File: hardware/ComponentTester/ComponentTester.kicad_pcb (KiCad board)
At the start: 2 copper layers, 51 x 90.6 mm, 18 parts, among them J1 Conn_01x06_Socket, J2 AVR-ISP-6, J3 Conn_02x07_Counter_Clockwise, J4 GameBoy_GamePak_DMG-09, SW1 SW_Push, U1 ATmega328P-A, X1 16MHz

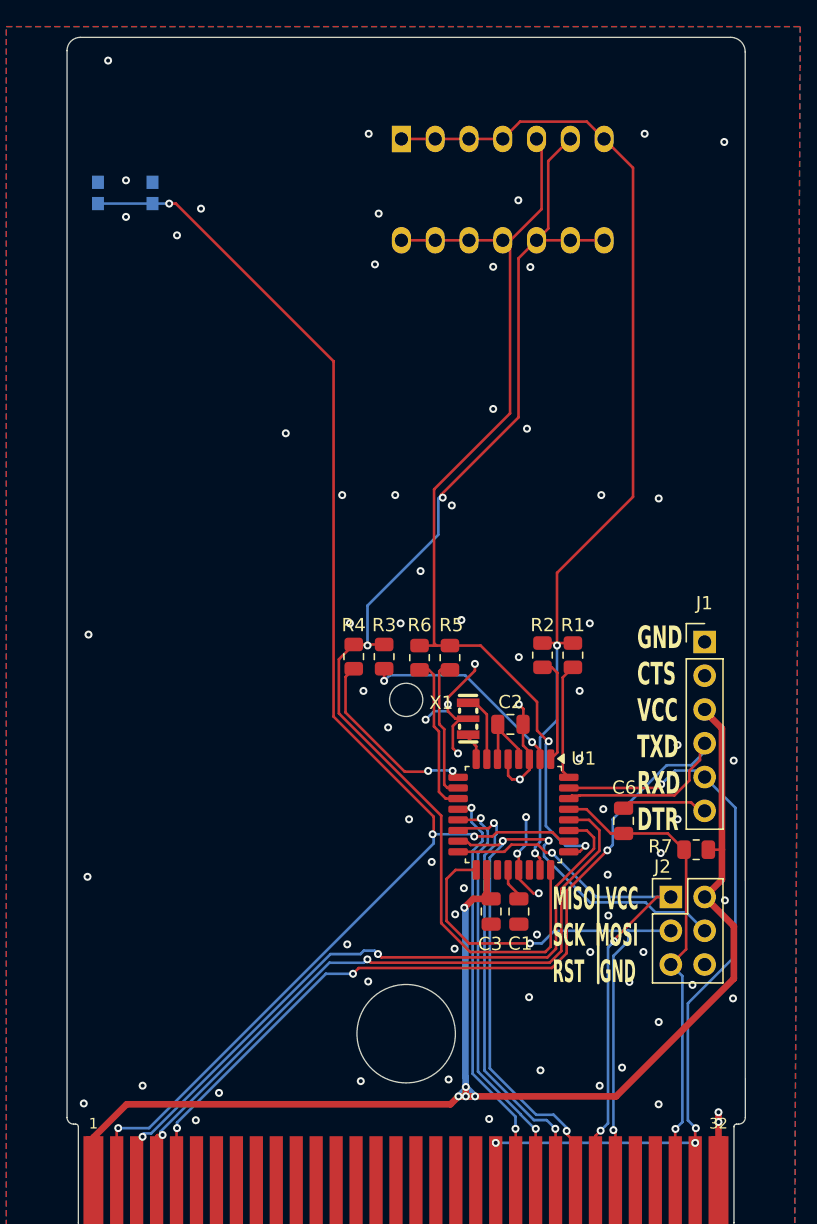
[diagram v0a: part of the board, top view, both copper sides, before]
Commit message: use ADC6 + ADC7
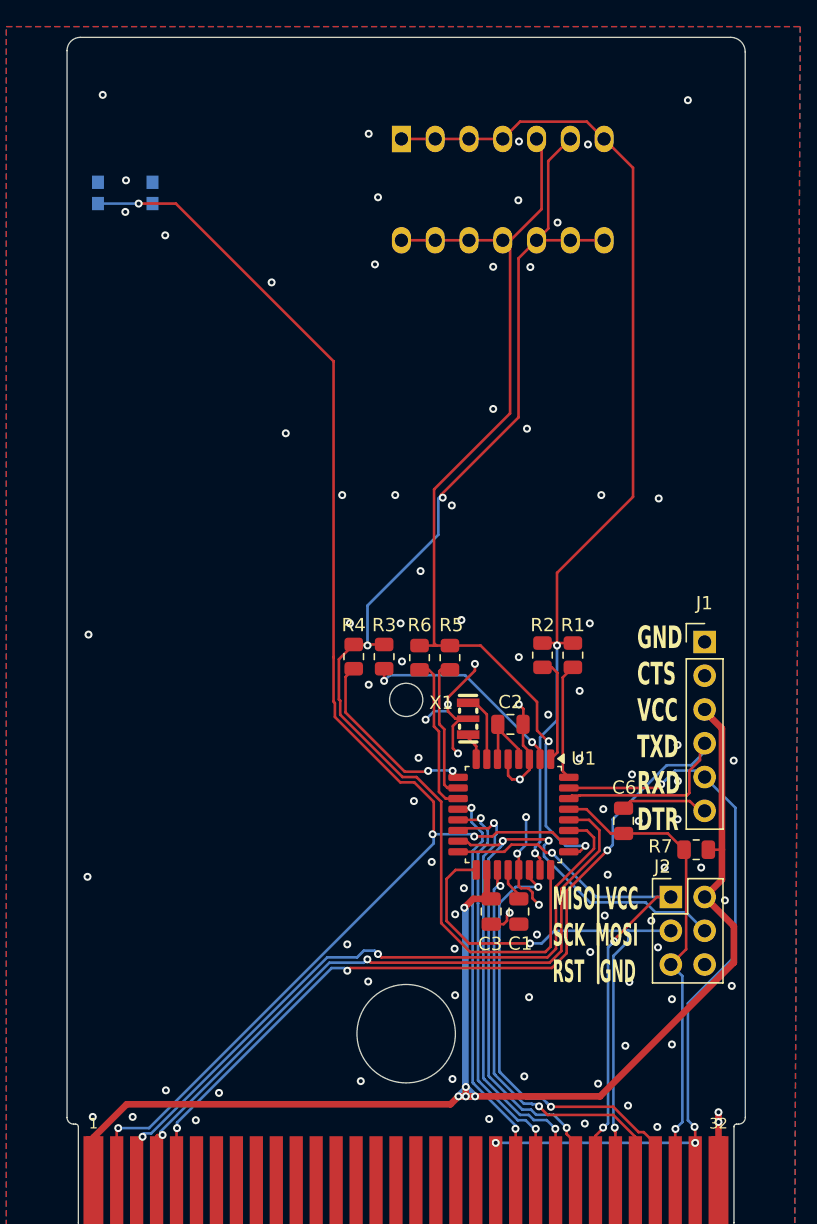
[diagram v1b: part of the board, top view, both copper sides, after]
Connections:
- U1 pad 19: unconnected-(U1-ADC6-Pad19) -> /CARD_D6
- U1 pad 22: unconnected-(U1-ADC7-Pad22) -> /CARD_D7
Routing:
- net /CARD_D7: track 0.00 -> 31.6 mm, vias 0 -> 2
- net /CARD_D6: track 0.00 -> 28.9 mm, vias 0 -> 2
- net GND: track 29.8 -> 32.7 mm, vias 78 -> 92
- net /CARD_~{CS}: track 69.9 -> 70.6 mm
- net /CARD_CLK: track 106.5 -> 107.1 mm
- net /2: track 91.8 -> 92.4 mm
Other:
- board text added: "Flash and program: https://electronoobs.com/eng_arduino_tut33.php https://wolles-elektronikkiste.de/atmega328p-standalone-betreiben"
- board text removed: "Flash and progran: https://electronoobs.com/eng_arduino_tut33.php"

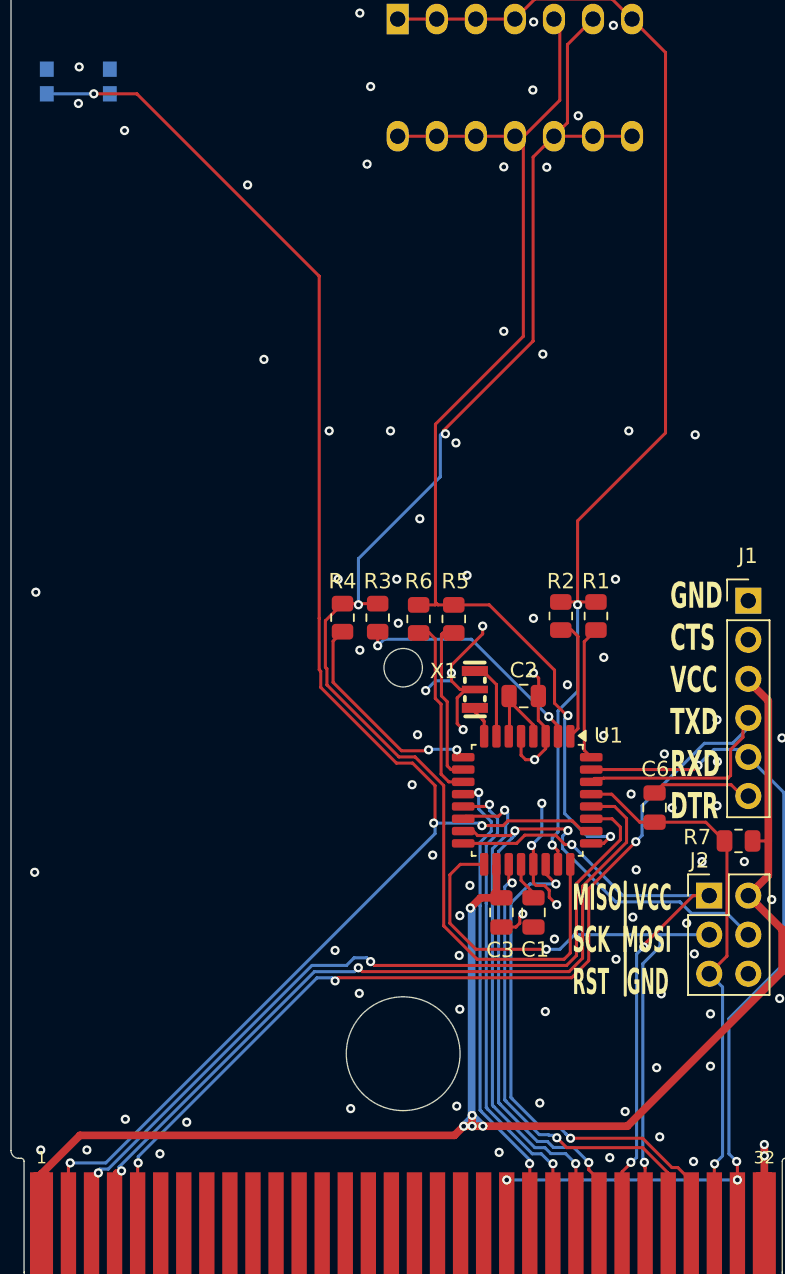
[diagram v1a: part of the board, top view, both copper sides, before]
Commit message: remove ext. crystal
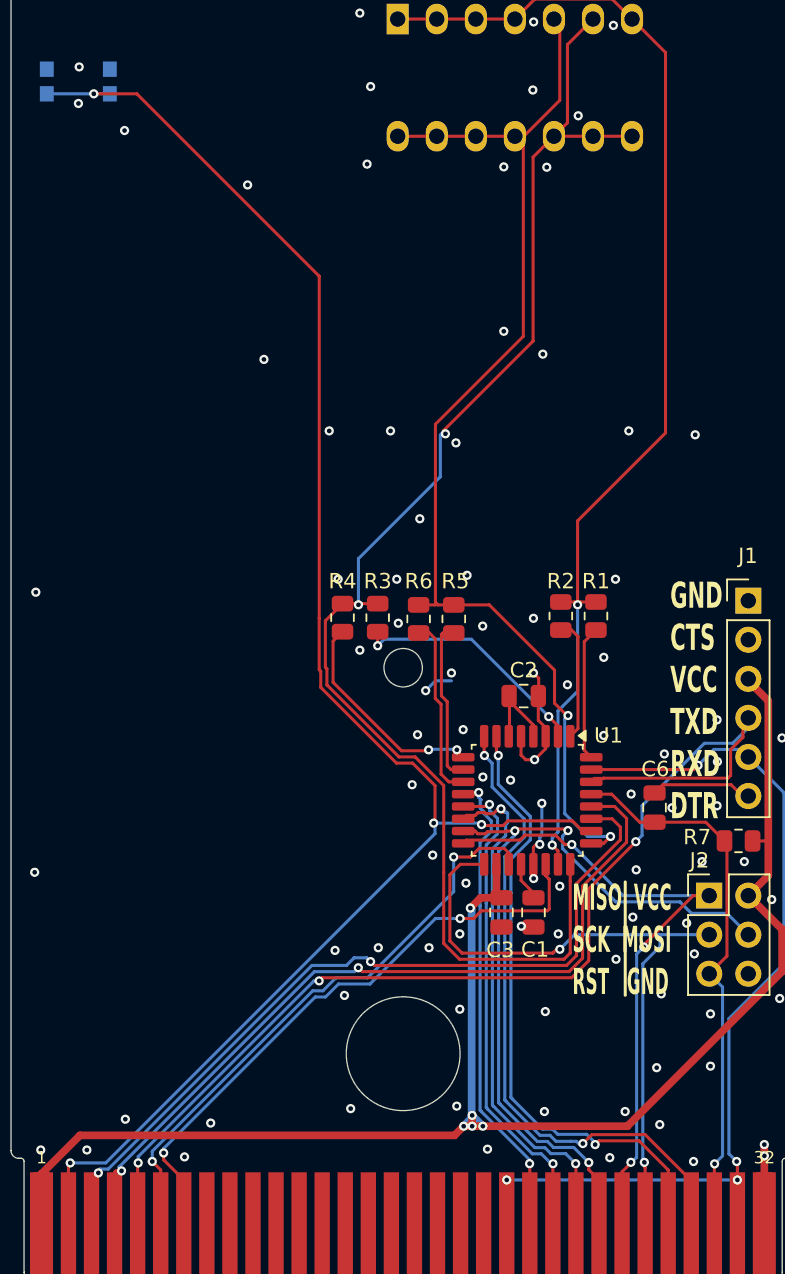
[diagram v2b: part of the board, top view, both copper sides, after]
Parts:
- removed X1: 16MHz, EasyEDA:OSC-SMD_3P-L3.2-W1.3-P1.2-L
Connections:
- U1 pad 19: /CARD_D6 -> /CARD_A0
- U1 pad 22: /CARD_D7 -> /CARD_A1
- U1 pad 7: Net-(U1-XTAL1/PB6) -> /CARD_D6
- U1 pad 8: Net-(U1-XTAL2/PB7) -> /CARD_D7
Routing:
- net /CARD_A1: track 0.00 -> 37.1 mm, vias 0 -> 2
- net /CARD_A0: track 0.00 -> 35.6 mm, vias 0 -> 2
- net GND: track 32.7 -> 17.4 mm, vias 92 -> 96
- net /CARD_D6: track 28.9 -> 38.0 mm
- net /CARD_D7: track 31.6 -> 40.1 mm
- net Net-(U1-XTAL1/PB6): track 5.13 -> 0.00 mm
- net Net-(U1-XTAL2/PB7): track 2.09 -> 0.00 mm
- net /CARD_CLK: track 107.1 -> 108.2 mm
- net /CARD_D5: track 40.1 -> 41.0 mm
- net /2: track 92.4 -> 93.0 mm
- net /CARD_D2: track 30.7 -> 31.2 mm

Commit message: clean up
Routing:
- net /1: track 77.8 -> 79.0 mm
- net /CARD_D2: track 31.2 -> 30.6 mm
- net GND: track 17.4 -> 17.2 mm, vias 96 -> 95

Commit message: some work
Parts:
- added J5: Conn_01x03_Pin, MyLibrary:Component_Testpad, B.Cu at (130.7, 61.4)
- moved R7 103.7 mm to (126.0, 104.6)
- moved J3 100.6 mm to (109.1, 61.3), turned to 90 degrees
- moved C6 98.4 mm to (126.0, 102.6), turned to 180 degrees
- moved C2 97.6 mm to (118.3, 95.8)
- moved C3 97.6 mm to (116.8, 109.8)
- moved J2 97.6 mm to (130.3, 108.7)
- moved J4 97.6 mm to (110.4, 134.7)
- moved R2 97.6 mm to (120.7, 90.6)
- moved U1 97.6 mm to (118.5, 102.6)
- moved C1 97.6 mm to (118.9, 109.8)
- moved R1 97.6 mm to (123.0, 90.6)
- moved R3 97.6 mm to (108.8, 90.7)
- moved R4 97.6 mm to (106.5, 90.7)
- moved R5 97.6 mm to (113.7, 90.8)
- moved R6 97.6 mm to (111.4, 90.8)
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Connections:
- C2 pad 1: Net-(C2-Pad1) -> +5V
- J3 pad 1: /1 -> /2
- J3 pad 10: /2 -> /1
- J3 pad 11: /3 -> /1
- J3 pad 13: /3 -> /2
- J3 pad 14: /3 -> /1
- J3 pad 2: /1 -> /2
- J3 pad 3: /1 -> /2
- J3 pad 4: /1 -> /3
- J3 pad 6: /2 -> /3
- J3 pad 7: /1 -> /3
- J3 pad 8: /2 -> /1
- J3 pad 9: /2 -> /1
- U1 pad 4: Net-(C2-Pad1) -> +5V
- U1 pad 6: Net-(C2-Pad1) -> +5V
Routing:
- net /1: track 79.0 -> 132.2 mm
- net /3: track 75.3 -> 112.3 mm
- net +5V: track 99.5 -> 135.3 mm, vias 5 -> 7
- net Net-(C2-Pad1): track 5.24 -> 0.00 mm
- net GND: track 17.2 -> 21.0 mm, vias 95 -> 140
- net /CARD_A1: track 37.1 -> 40.2 mm
- net /CARD_D5: track 41.0 -> 43.8 mm, vias 2 -> 4
- net /CARD_CLK: track 108.2 -> 110.7 mm, vias 4 -> 5
- net /CARD_A0: track 35.6 -> 38.0 mm
- net /2: track 93.0 -> 95.3 mm
- net Net-(U1-PD4): track 15.8 -> 18.1 mm
- net /CARD_~{RD}: track 50.2 -> 48.7 mm
- net /CARD_~{CS}: track 70.4 -> 69.0 mm
- net /CARD_~{WR}: track 49.8 -> 48.4 mm
- net /CARD_D2: track 30.6 -> 29.4 mm
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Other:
- outline, holes or cut-outs redrawn
- board text added: "2 5"
- board text added: "3 9"
- board text added: "PCB Thickness: 0.8mm!!"
- board text added: "jsc69@gmx.de"
- board text removed: "Flash and program: https://electronoobs.com/eng_arduino_tut33.php https://wolles-elektronikkiste.de/atmega328p-standalone-betreiben"

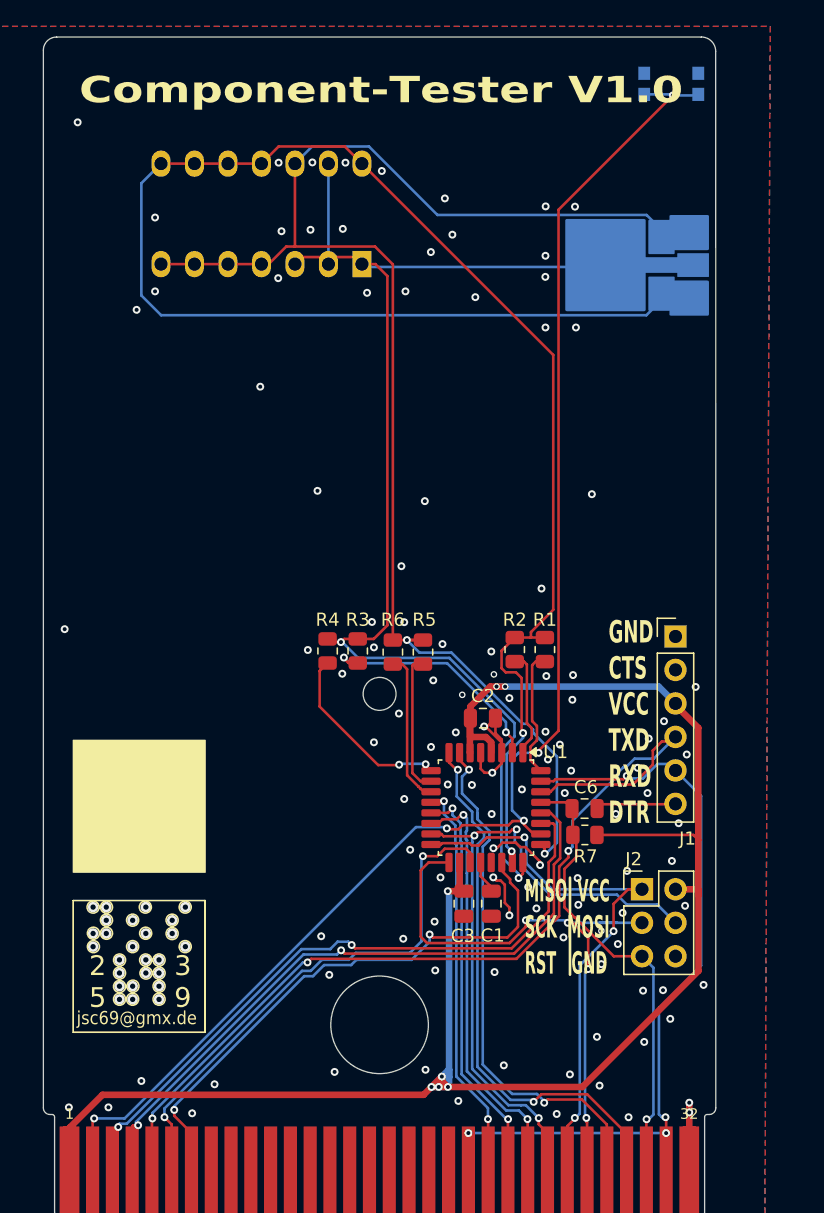
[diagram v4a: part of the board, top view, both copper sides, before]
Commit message: replace ATmega328P with ATmegaPB
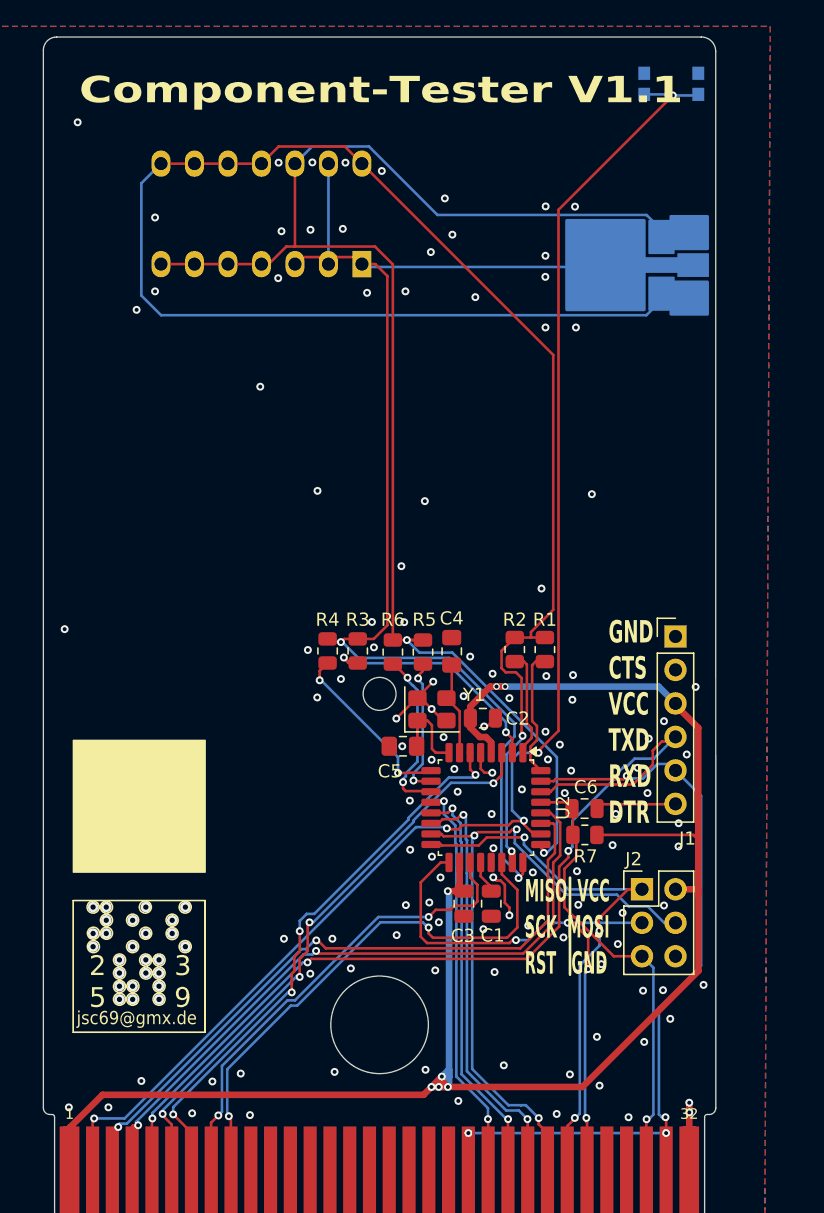
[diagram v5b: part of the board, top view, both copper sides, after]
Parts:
- removed U1: ATmega328P-A, Package_QFP:TQFP-32_7x7mm_P0.8mm
- added C4: 22pF, Capacitor_SMD:C_0805_2012Metric_Pad1.18x1.45mm_HandSolder, F.Cu at (115.9, 90.7)
- added C5: 22pF, Capacitor_SMD:C_0805_2012Metric_Pad1.18x1.45mm_HandSolder, F.Cu at (112.2, 97.9)
- added U2: ATmega328PB-A, Package_QFP:TQFP-32_7x7mm_P0.8mm, F.Cu at (118.5, 102.6)
- added Y1: 16MHz, Crystal:Crystal_SMD_3225-4Pin_3.2x2.5mm, F.Cu at (114.4, 95.1)
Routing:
- net /CARD_D7: track 39.1 -> 0.00 mm, vias 2 -> 0
- net /CARD_A3: track 0.00 -> 38.2 mm, vias 0 -> 2
- net /CARD_D6: track 37.6 -> 0.00 mm, vias 2 -> 0
- net /CARD_A2: track 0.00 -> 33.2 mm, vias 0 -> 2
- net Net-(U2-XTAL1/PB6): track 0.00 -> 7.23 mm
- net Net-(U2-XTAL2/PB7): track 0.00 -> 6.44 mm
- net GND: track 21.0 -> 16.2 mm, vias 140 -> 147
- net /CARD_A0: track 38.0 -> 42.3 mm, vias 2 -> 4
- net +5V: track 135.3 -> 132.2 mm
- net /CARD_D5: track 43.8 -> 41.5 mm
- net Net-(U2-PD7): track 11.6 -> 12.9 mm, vias 0 -> 2
- net /CARD_D4: track 40.6 -> 39.8 mm
- net /CARD_D3: track 49.1 -> 48.4 mm
- net /CARD_A1: track 40.2 -> 40.8 mm, vias 2 -> 4
- net Net-(U2-PD6): track 10.7 -> 10.8 mm, vias 0 -> 2
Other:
- board text added: "Component-Tester V1.1"
- board text removed: "Component-Tester V1.0"
